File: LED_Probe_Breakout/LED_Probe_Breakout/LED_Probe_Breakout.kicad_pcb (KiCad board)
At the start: 4 copper layers, 119.5 x 103 mm, 25 parts, among them J1 Conn_01x40, J10 Conn_Coaxial, J11 Conn_Coaxial, J12 Conn_Coaxial, J13 Conn_Coaxial, J14 Conn_Coaxial, J15 Conn_Coaxial, J16 Conn_Coaxial, J17 Conn_Coaxial, J18 Conn_01x04_Socket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

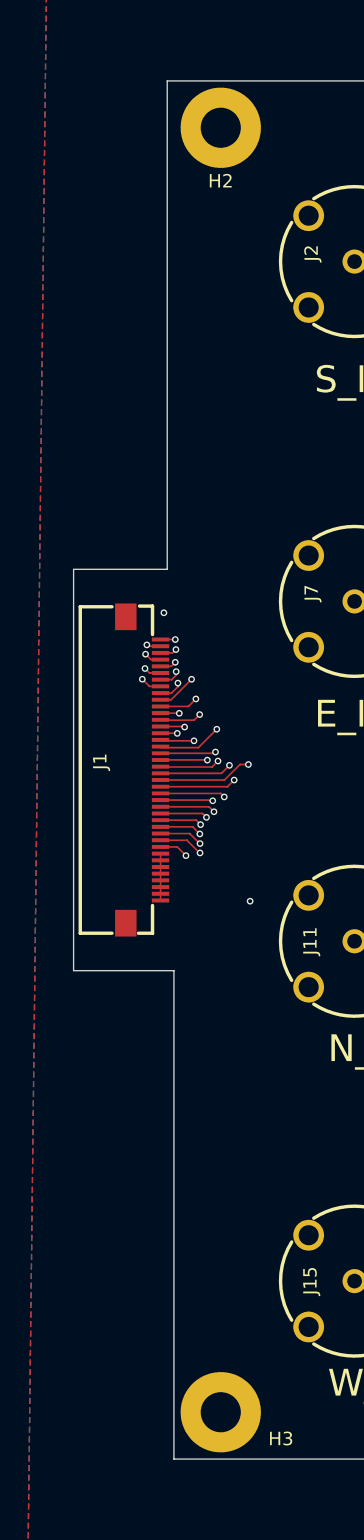
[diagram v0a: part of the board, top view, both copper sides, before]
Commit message: update to 2x 20P
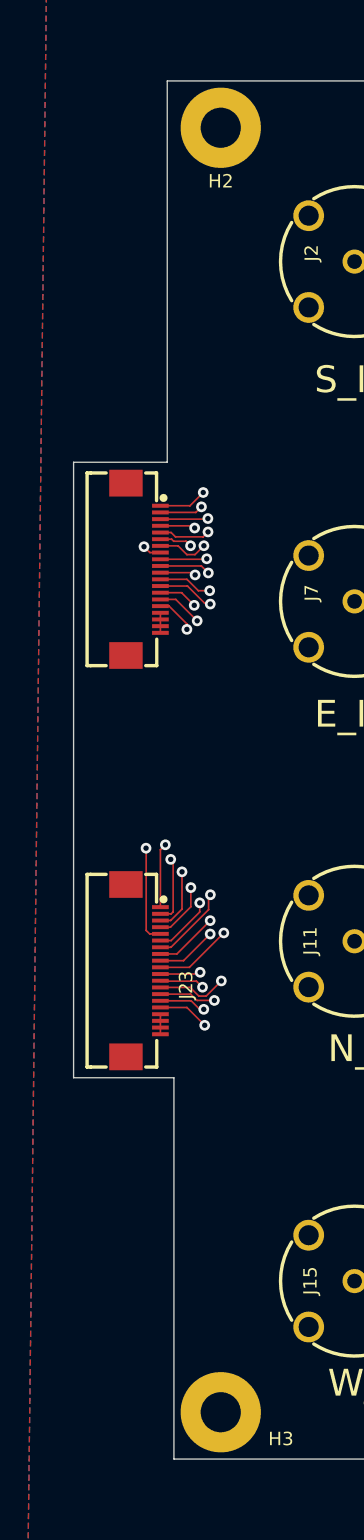
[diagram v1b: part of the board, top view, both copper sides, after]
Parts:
- removed J1: Conn_01x40, 0_Breakout_footprint_lib:FPC-SMD_P0.50-40P_FGS-XJ-H2.0
- added J22: Conn_01x22, 0_Breakout_footprint_lib:FPC-SMD_20P-P0.50_XUNPU_FPC-05F-20PH20, F.Cu at (-50.8, 23.0)
- added J23: Conn_01x22, 0_Breakout_footprint_lib:FPC-SMD_20P-P0.50_XUNPU_FPC-05F-20PH20, F.Cu at (-50.8, 53.0)
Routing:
- net /Solder_Point_Breakout/Sig_4: track 154.2 -> 139.1 mm
- net /Solder_Point_Breakout/Sig_3: track 149.1 -> 135.2 mm
- net /W_V+: track 88.5 -> 76.6 mm
- net /W_I-: track 54.1 -> 42.3 mm
- net /Solder_Point_Breakout3/Sig_4: track 138.1 -> 126.5 mm
- net /Solder_Point_Breakout2/Sig_1: track 108.8 -> 120.2 mm
- net /N_V-: track 90.4 -> 101.4 mm
- net /Solder_Point_Breakout/Sig_2: track 141.1 -> 130.2 mm
- net /Solder_Point_Breakout/Sig_1: track 133.9 -> 123.3 mm
- net /N_V+: track 71.2 -> 81.8 mm
- net /Solder_Point_Breakout2/Sig_2: track 110.0 -> 120.1 mm
- net /W_V-: track 107.4 -> 97.5 mm, vias 2 -> 1
- net /Solder_Point_Breakout2/Sig_4: track 112.5 -> 122.0 mm
- net /S_I+: track 39.7 -> 30.2 mm
- net /Solder_Point_Breakout2/Sig_3: track 111.1 -> 120.4 mm
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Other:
- outline, holes or cut-outs redrawn

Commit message: Breakout Board update
flipped connector pinout
made connectors inline
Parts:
- moved J22 31.4 mm to (-78.4, 38.0)
- moved J23 15.2 mm to (-53.0, 38.0)
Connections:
- J22 pad 1: /S_I+ -> GND
- J22 pad 10: /Solder_Point_Breakout1/Sig_1 -> /E_V+
- J22 pad 11: /E_V+ -> /Solder_Point_Breakout1/Sig_1
- J22 pad 12: /Solder_Point_Breakout1/Sig_2 -> /E_I+
- J22 pad 13: /E_V- -> /Solder_Point_Breakout/Sig_4
- J22 pad 14: /Solder_Point_Breakout1/Sig_3 -> /S_I-
- J22 pad 15: /E_I- -> /Solder_Point_Breakout/Sig_3
- J22 pad 16: /Solder_Point_Breakout1/Sig_4 -> /S_V-
- J22 pad 17: GND -> /Solder_Point_Breakout/Sig_2
- J22 pad 18: GND -> /S_V+
- J22 pad 19: GND -> /Solder_Point_Breakout/Sig_1
- J22 pad 2: /Solder_Point_Breakout/Sig_1 -> GND
- J22 pad 20: GND -> /S_I+
- J22 pad 3: /S_V+ -> GND
- J22 pad 4: /Solder_Point_Breakout/Sig_2 -> GND
- J22 pad 5: /S_V- -> /Solder_Point_Breakout1/Sig_4
- J22 pad 6: /Solder_Point_Breakout/Sig_3 -> /E_I-
- J22 pad 7: /S_I- -> /Solder_Point_Breakout1/Sig_3
- J22 pad 8: /Solder_Point_Breakout/Sig_4 -> /E_V-
- J22 pad 9: /E_I+ -> /Solder_Point_Breakout1/Sig_2
- J23 pad 1: /N_I+ -> GND
- J23 pad 10: /Solder_Point_Breakout3/Sig_1 -> /W_V+
- J23 pad 11: /W_V+ -> /Solder_Point_Breakout3/Sig_1
- J23 pad 12: /Solder_Point_Breakout3/Sig_2 -> /W_I+
- J23 pad 13: /W_V- -> /Solder_Point_Breakout2/Sig_4
- J23 pad 14: /Solder_Point_Breakout3/Sig_3 -> /N_I-
- J23 pad 15: /W_I- -> /Solder_Point_Breakout2/Sig_3
- J23 pad 16: /Solder_Point_Breakout3/Sig_4 -> /N_V-
- J23 pad 17: GND -> /Solder_Point_Breakout2/Sig_2
- J23 pad 18: GND -> /N_V+
- J23 pad 19: GND -> /Solder_Point_Breakout2/Sig_1
- J23 pad 2: /Solder_Point_Breakout2/Sig_1 -> GND
- J23 pad 20: GND -> /N_I+
- J23 pad 3: /N_V+ -> GND
- J23 pad 4: /Solder_Point_Breakout2/Sig_2 -> GND
- J23 pad 5: /N_V- -> /Solder_Point_Breakout3/Sig_4
- J23 pad 6: /Solder_Point_Breakout2/Sig_3 -> /W_I-
- J23 pad 7: /N_I- -> /Solder_Point_Breakout3/Sig_3
- J23 pad 8: /Solder_Point_Breakout2/Sig_4 -> /W_V-
- J23 pad 9: /W_I+ -> /Solder_Point_Breakout3/Sig_2
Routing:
- net /S_V-: track 105.1 -> 173.0 mm
- net /S_I-: track 54.0 -> 118.9 mm
- net /S_I+: track 30.2 -> 92.4 mm
- net /S_V+: track 84.3 -> 145.7 mm
- net /Solder_Point_Breakout/Sig_1: track 123.3 -> 183.2 mm
- net /Solder_Point_Breakout/Sig_2: track 130.2 -> 188.0 mm
- net /Solder_Point_Breakout1/Sig_1: track 108.3 -> 164.7 mm
- net /Solder_Point_Breakout/Sig_3: track 135.2 -> 190.5 mm
- net /Solder_Point_Breakout/Sig_4: track 139.1 -> 192.9 mm
- net /Solder_Point_Breakout3/Sig_4: track 126.5 -> 174.4 mm
- net /Solder_Point_Breakout1/Sig_2: track 107.4 -> 152.8 mm
- net /Solder_Point_Breakout1/Sig_3: track 108.0 -> 151.1 mm
- net /Solder_Point_Breakout3/Sig_3: track 130.1 -> 169.4 mm
- net /E_V+: track 71.0 -> 109.9 mm
- net /E_I+: track 15.8 -> 54.5 mm
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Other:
- board size 119.5 x 103 mm -> 147.1 x 103 mm
